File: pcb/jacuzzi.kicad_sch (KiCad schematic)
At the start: 75 parts, among them J1 Conn_01x03, J10 Conn_01x02, J11 Conn_01x03, J12 Conn_01x04, J2 Conn_01x03, J3 Conn_01x03, J4 Conn_01x04, J5 Conn_01x03, J6 Conn_01x03, J7 Conn_01x02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

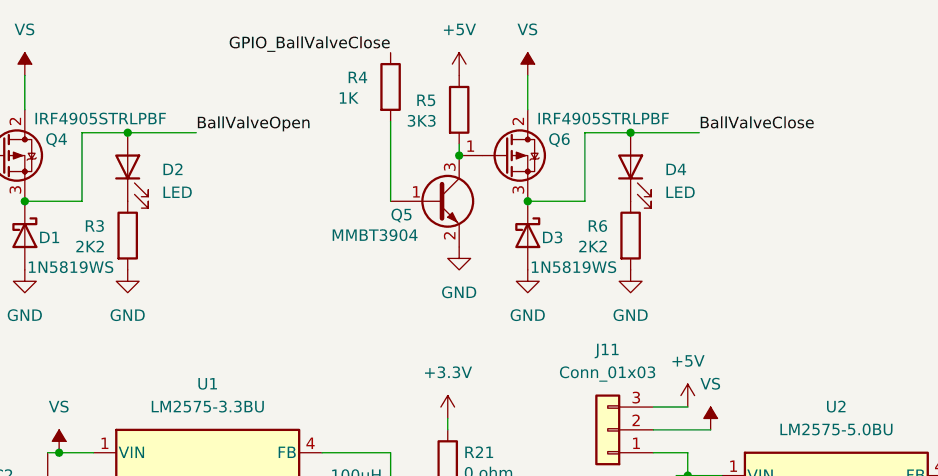
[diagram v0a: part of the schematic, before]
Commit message: add missing footprints
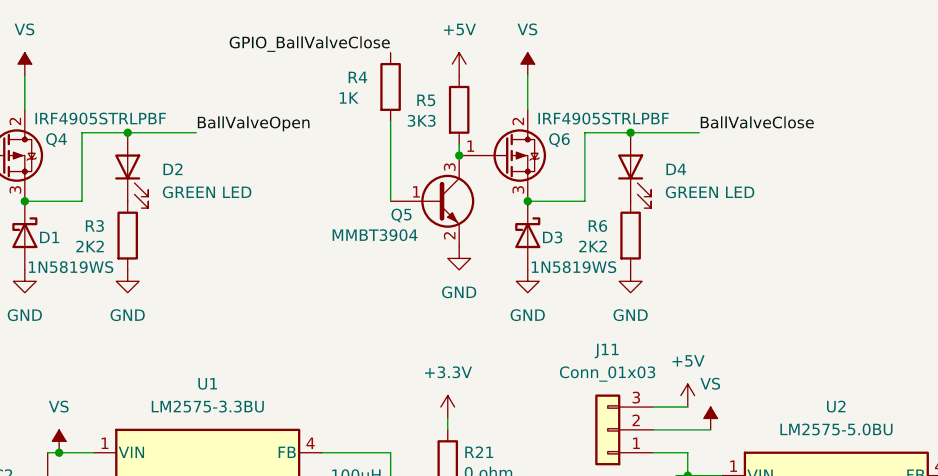
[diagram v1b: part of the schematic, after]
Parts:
- D11, D13: footprint (none) -> LED_SMD:LED_0805_2012Metric
- D2, D4: value LED -> GREEN LED; footprint (none) -> LED_SMD:LED_0805_2012Metric
- J10, J7: footprint (none) -> Connector_Phoenix_MC:PhoenixContact_MCV_1,5_2-G-3.81_1x02_P3.81mm_Vertical

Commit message: started layout
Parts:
- removed J12: Conn_01x04, Connector_PinHeader_2.54mm:PinHeader_1x04_P2.54mm_Vertical_SMD_Pin1Left, symbol Connector_Generic:Conn_01x04
- removed J4: Conn_01x04, Connector_PinSocket_2.54mm:PinSocket_1x04_P2.54mm_Vertical_SMD_Pin1Left, symbol Connector_Generic:Conn_01x04
- removed R17, R18, R19, R20: 1K1, Resistor_SMD:R_0805_2012Metric, symbol Device:R
- added D22, D23, D25, D26: BAT54S, Package_TO_SOT_SMD:SOT-23, symbol Diode:BAT54S
- added J13, J14, J15, J16: Conn_01x01, Connector:IHI_B6A-PCB-45_Vertical, symbol Connector_Generic:Conn_01x01
- added J4: Conn_01x05, Connector_JST:JST_SH_BM04B-SRSS-TB_1x04-1MP_P1.00mm_Vertical, symbol Connector_Generic:Conn_01x05
- added U4: DM-OLED096-636, DM-OLED096-636:MODULE_DM-OLED096-636, symbol DM-OLED096-636:DM-OLED096-636
- J8: footprint Connector_PinHeader_2.54mm:PinHeader_1x08_P2.54mm_Vertical_SMD_Pin1Left -> Connector_PinHeader_2.54mm:PinHeader_1x08_P2.54mm_Vertical
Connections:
- net +3.3V: now also D22.2 (K), D23.2 (K), D25.2 (K), D26.2 (K), J4.1 (Pin_1)
- net +5V: now also U4.2 (VCC_IN)
- net GND: now also D22.1 (A), D23.1 (A), D25.1 (A), D26.1 (A), J4.2 (Pin_2), J4.5 (Pin_5), U4.1 (GND)
- net GPIO_I2C_SCL: now also J4.4 (Pin_4), U4.3 (SCL)
- net GPIO_I2C_SDA: now also J4.3 (Pin_3), U4.4 (SDA)
- net TubValve_NO: now also J3.1 (Pin_1); no longer J3.2 (Pin_2)
- net TubValve_V: now also J3.2 (Pin_2); no longer J3.1 (Pin_1)
- net GPIO_ADC8: now reaches U3.23 (IO15)
- net GPIO_ADC8: now also D26.3 (COM), J16.1 (Pin_1)
- net GPIO_ADC7: now reaches U3.24 (IO2)
- net GPIO_ADC7: now also D23.3 (COM), J15.1 (Pin_1)
- net GPIO_ADC6: now reaches U3.25 (IO0)
- net GPIO_ADC6: now also D25.3 (COM), J13.1 (Pin_1)
- net GPIO_ADC5: now reaches U3.26 (IO4)
- net GPIO_ADC5: now also D22.3 (COM), J14.1 (Pin_1)

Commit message: started layout
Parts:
- J4: footprint Connector_JST:JST_SH_BM04B-SRSS-TB_1x04-1MP_P1.00mm_Vertical -> Connector_JST:JST_SH_SM04B-SRSS-TB_1x04-1MP_P1.00mm_Horizontal
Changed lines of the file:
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@@
 			)
 		)
-		(property "Footprint" "Connector_JST:JST_SH_BM04B-SRSS-TB_1x04-1MP_P1.00mm_Vertical"
+		(property "Footprint" "Connector_JST:JST_SH_SM04B-SRSS-TB_1x04-1MP_P1.00mm_Horizontal"
 			(at 189.23 161.29 0)
 			(effects

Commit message: started on bom
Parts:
- D10, D12, D14, D15, D16, D17, D18, D19, D22, D23, D24, D25, D26, D6, D7, D8, D9: LCSC (none) -> C916425
- D11, D13, D2, D4: LCSC (none) -> C434435
- J1, J2, J5, J6: LCSC (none) -> C480525
- J10, J7: LCSC (none) -> C480514
- J11: LCSC (none) -> C5160786
- J3: LCSC (none) -> C480509
- J4: LCSC (none) -> C189895
- L1: LCSC (none) -> C169378
- L2: LCSC (none) -> C169381
- Q1, Q2, Q3, Q5: LCSC (none) -> C2891808
- Q4, Q6: LCSC (none) -> C2620
- U1: LCSC (none) -> C347404
- U2: LCSC (none) -> C316680
- U4: LCSC (none) -> C5248080

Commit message: add diode for 3v and 5v, missing markings on pcb
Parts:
- added D27: 5V, LED_SMD:LED_0805_2012Metric, symbol Device:LED
- added D28: 3.3V, LED_SMD:LED_0805_2012Metric, symbol Device:LED
- added R17, R18: 300R, Resistor_SMD:R_0805_2012Metric, symbol Device:R
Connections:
- net +3.3V: now also R18.2
- net +5V: now also R17.2
- net GND: now also D27.1 (K), D28.1 (K)
- new net: D28.2 (A), R18.1
- new net: D27.2 (A), R17.1

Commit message: add transistor to drive 5v on relay
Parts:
- removed J4: Conn_01x05, Connector_JST:JST_SH_SM04B-SRSS-TB_1x04-1MP_P1.00mm_Horizontal, symbol Connector_Generic:Conn_01x05
- added J4: Conn_02x02_Counter_Clockwise_MountingPin, Connector_JST:JST_SH_SM04B-SRSS-TB_1x04-1MP_P1.00mm_Horizontal, symbol Connector_Generic_MountingPin:Conn_02x02_Counter_Clockwise_MountingPin
- added Q7: MMBT3904, Package_TO_SOT_SMD:SOT-23, symbol Transistor_BJT:MMBT3904
- added R19: 1K, Resistor_SMD:R_0805_2012Metric, symbol Device:R
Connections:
- net +3.3V: now also J4.1 (Pin_1)
- net +5V: now also D5.1 (K), K1.2
- net GND: now also J4.2 (Pin_2), J4.MP (MountPin), Q7.2 (E); no longer D5.2 (A), K1.5
- net GPIO_I2C_SCL: now also J4.4 (Pin_4)
- net GPIO_I2C_SDA: now also J4.3 (Pin_3)
- net GPIO_TubValve: now also R19.1; no longer D5.1 (K), K1.2
- new net: Q7.1 (B), R19.2
- new net: D5.2 (A), K1.5, Q7.3 (C)

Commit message: now with all parts defined
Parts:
- C1: LCSC (none) -> C15850
- C2, C4: LCSC (none) -> C116241
- C3, C5: LCSC (none) -> C74623
- D1, D20, D21, D3, D5: LCSC (none) -> C191023
- J8: LCSC (none) -> C376081
- J9: LCSC (none) -> C668623
- K1: value G5LE-1 -> SRD-05VDC; footprint Relay_THT:Relay_SPDT_Omron-G5LE-1 -> Relay_THT:Relay_SPDT_SANYOU_SRD_Series_Form_C; LCSC (none) -> C35449
- R1, R11, R14, R19, R4: LCSC (none) -> C17513
- R10, R2, R5, R7, R8, R9: LCSC (none) -> C26010
- R12, R15, R17, R18: LCSC (none) -> C25304
- R13, R16, R27: LCSC (none) -> C17414
- R21: LCSC (none) -> C17477
- R23, R24: LCSC (none) -> C27834
- R3, R6: LCSC (none) -> C2907303

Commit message: ordered
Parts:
- removed J13, J14, J15, J16: Conn_01x01, Connector:IHI_B6A-PCB-45_Vertical, symbol Connector_Generic:Conn_01x01
- added J12, J19: Conn_01x03, Connector_Phoenix_MC:PhoenixContact_MCV_1,5_3-G-3.81_1x03_P3.81mm_Vertical, symbol Connector_Generic:Conn_01x03
- added R20, R22: 3K3, Resistor_SMD:R_0805_2012Metric, symbol Device:R
- added TP1, TP2, TP3, TP4: TestPoint, TestPoint:TestPoint_Pad_D4.0mm, symbol Connector:TestPoint
- D11, D13, D2, D27, D28, D4: LCSC C434435 -> C2296
- J8: value Conn_01x08 -> Conn_01x06; footprint Connector_PinHeader_2.54mm:PinHeader_1x08_P2.54mm_Vertical -> Connector_PinHeader_2.54mm:PinHeader_1x06_P2.54mm_Vertical; symbol Connector_Generic:Conn_01x08 -> Connector_Generic:Conn_01x06; LCSC C376081 -> C37208
- R12, R15, R17, R18: LCSC C25304 -> C17617
- R3, R6: LCSC C2907303 -> C17520
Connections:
- net +3.3V: now also R20.1, R22.1
- net +5V: now also C2.1, U1.1 (VIN), J12.1 (Pin_1), J19.1 (Pin_1)
- net BallValveClose: now also Q6.2 (D), R6.1; no longer D4.2 (A), Q6.3 (S)
- net BallValveOpen: now also Q4.2 (D), R3.1; no longer D2.2 (A), Q4.3 (S)
- net GND: now also D2.1 (K), D4.1 (K), J8.6 (Pin_6), J12.3 (Pin_3), J19.3 (Pin_3); no longer J8.8 (Pin_8), R3.2, R6.2
- net GPIO10: now also J19.2 (Pin_2), R22.2; no longer J8.7 (Pin_7)
- net GPIO9: now also J12.2 (Pin_2), R20.2; no longer J8.6 (Pin_6)
- net GPIO_ADC5: now also TP2.1
- net GPIO_ADC6: now also TP1.1
- net GPIO_ADC7: now also TP3.1
- net GPIO_ADC8: now also TP4.1
- net VS: now also Q4.3 (S), Q6.3 (S); no longer C2.1, Q4.2 (D), Q6.2 (D), U1.1 (VIN)
- new net: D4.2 (A), R6.2
- new net: D2.2 (A), R3.2
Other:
- moved on the sheet: D1, D24, D3, D4, Q4, Q5, Q6, R1, R27, R6
